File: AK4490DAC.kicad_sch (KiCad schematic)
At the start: 35 parts, among them IC1 LP5907MFX-3.3/NOPB, IC2 LP5907MFX-3.3/NOPB, IC3 LP5907MFX-3.3/NOPB, IC4 TPS7A2050PDBVR, IC5 MUSES8920, IC6 MUSES8920, IC7 MUSES8920, IC8 TPS7A2050PDBVR, IC9 AMS1117, J1 JST_XA_B02B-XASK-1, Q1 BSS138, T1 DA103C, U1 SN74LS06NSR, U3 TCM809RENB713, U4 TCM809RENB713, U5 AK4118, U6 AK4490, Y1 11.2896MHz

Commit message: Add PCM2704C USB input circuit with transformer isolation from AK4118
Places (unwired, matching this project's existing convention for
support components -- see the wiring table below) all parts needed for
the "SPDIF primary, USB via jumper" architecture:

PCM2704C USB Audio DAC (bus-powered, isolated USB-side domain):
- U2: PCM2704CDBR
- Y2 + C14/C15: 12MHz crystal w/ 22pF load caps (TI SBFS036A Fig.34)
- C16-C19: 1uF decoupling on VDD/VCCL/VCCR/VCCP
- C20: 10uF on VCOM
- R5: 1.5k D+ pullup to VCCP (full-speed device)
- R6/R7: 22R series termination on D+/D-
- J2: USB_B_Micro connector (VBUS/D+/D-/GND from USB, own USB_GND
  domain -- do NOT tie to main board GND)

Galvanic isolation network (reusing the already-placed T1/DA103C,
matching the original NEWDAC transformer-isolation topology):
- R8: 240R series from PCM2704C DOUT into T1 primary
- R9: 120R primary-side shunt/termination (USB_GND referenced)
- C21: 0.1uF DC block on T1 secondary
- R10: 75R secondary-side termination to main GND, mirroring the
  existing RX0 network's R2=75R (AK4118 datasheet Fig.21 pattern)

AK4118 RX channel select jumper:
- JP1: 3-pin header on IPS0 -- pin1=GND selects RX0 (external SPDIF
  input), pin3=+3V3_118 selects RX1 (PCM2704C via the isolation xfmr)

External SPDIF input jack:
- J3: 2-pin generic connector feeding the existing RX0 coupling
  network (C4/R2), placeholder footprint -- swap for the actual RCA
  or Toslink part footprint once chosen

New lib_symbols cache entries added: Connector_Generic:Conn_01x03,
Connector:USB_B_Micro (both extracted verbatim from KiCad's global
libraries, same safe methodology as the earlier LP5907/TPS7A20 fixes).

Bug found and fixed during this work: the Conn_01x03 block extracted
from the global library keeps its bare name ("Conn_01x03") instead of
the library-qualified name used by lib_id references
("Connector_Generic:Conn_01x03"). Instantiating a part against that
mismatched cache entry reproducibly segfaults kicad-cli sch erc --
same f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
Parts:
- added C14, C15: 22pF, Capacitor_SMD:C_0603_1608Metric, symbol Device:C
- added C16, C17, C18, C19: 1uF, Capacitor_SMD:C_0603_1608Metric, symbol Device:C
- added C20: 10uF, Capacitor_SMD:C_0805_2012Metric, symbol Device:C
- added C21: 0.1uF, Capacitor_SMD:C_0603_1608Metric, symbol Device:C
- added J2: USB_B_Micro, Connector_USB:USB_Micro-B_Molex-105017-0001, symbol Connector:USB_B_Micro
- added J3: SPDIF_IN, symbol Connector_Generic:Conn_01x02
- added JP1: IPS0_SEL, Connector_PinHeader_2.54mm:PinHeader_1x03_P2.54mm_Vertical, symbol Connector_Generic:Conn_01x03
- added R10: 75, Resistor_SMD:R_0603_1608Metric, symbol Device:R
- added R5: 1.5k, Resistor_SMD:R_0603_1608Metric, symbol Device:R
- added R6, R7: 22, Resistor_SMD:R_0603_1608Metric, symbol Device:R
- added R8: 240, Resistor_SMD:R_0603_1608Metric, symbol Device:R
- added R9: 120, Resistor_SMD:R_0603_1608Metric, symbol Device:R
- added U2: PCM2704CDBR, Package_SO:SSOP-28_5.3x10.2mm_P0.65mm, symbol AK4490DAC:PCM2704CDBR
- added Y2: 12MHz, Crystal:Crystal_SMD_3225-4Pin_3.2x2.5mm, symbol Device:Crystal

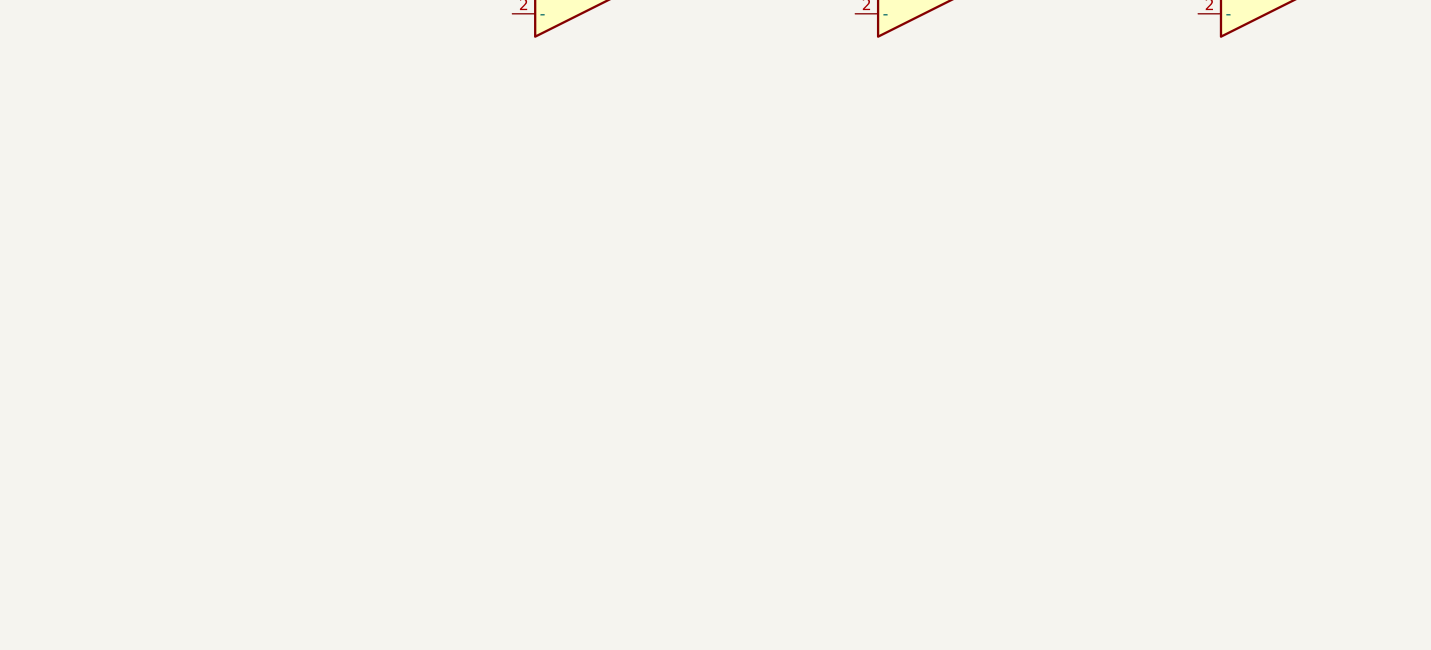
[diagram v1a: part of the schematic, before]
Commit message: Add AK4490 differential I/V + diff-amp output stage components
Places (unwired, per this project's convention) the analog output
stage feeding off the already-placed IC5/IC6/IC7 (MUSES8920 dual
op-amps) and Q1 (BSS138), using the AK4490's real differential current
output pins (AOUTLP/AOUTLN/VCML and AOUTRP/AOUTRN/VCMR, per the
pin-verified symbol) instead of a single-ended assumption.

Topology: 3 op-amp units per channel (I/V converter x2 + differential
combiner x1), which maps exactly onto the 3 existing dual-op-amp
packages:
  IC5 (A,B) -> L channel I/V converters (AOUTLP, AOUTLN)
  IC6 (A)   -> L channel differential-to-single-ended combiner
  IC6 (B)   -> R channel I/V converter (AOUTRP)
  IC7 (A)   -> R channel I/V converter (AOUTRN)
  IC7 (B)   -> R channel differential-to-single-ended combiner

New parts per channel:
- 2x 1k transimpedance feedback R (I/V conversion) + 2x 100pF parallel
  feedback C (HF stability)
- 4x 10k matched-resistor differential amplifier network (unity gain)
- 1x 1uF output DC-block coupling cap
- J4/J5: line-out connectors (L/R), placeholder footprint

Verified via kicad-cli sch erc: 377 violations, lib_symbol_mismatch=5
(unchanged baseline), no new violation categories, no crash.

Values (1k I/V, 100pF, 10k diff network, 1uF coupling) are reasonable
starting points, not simulated/verified against the AK4490 datasheet's
own reference application figure -- recommend double-checking against
that figure (output swing vs. AK4490's full-scale output current)
before finalizing for fab.

Still pending: net wiring for this stage and everything else placed so
far (left for manual wiring per this project's established pattern),
plus the remaining static AK4118/AK4490 mode-select pin ties.

Co-Authored-By: Claude Sonnet 5 <noreply@anthropic.com>
Claude-Session: https://claude.ai/code/session_01UHxU1bYnUhoAmCyc4Koj96
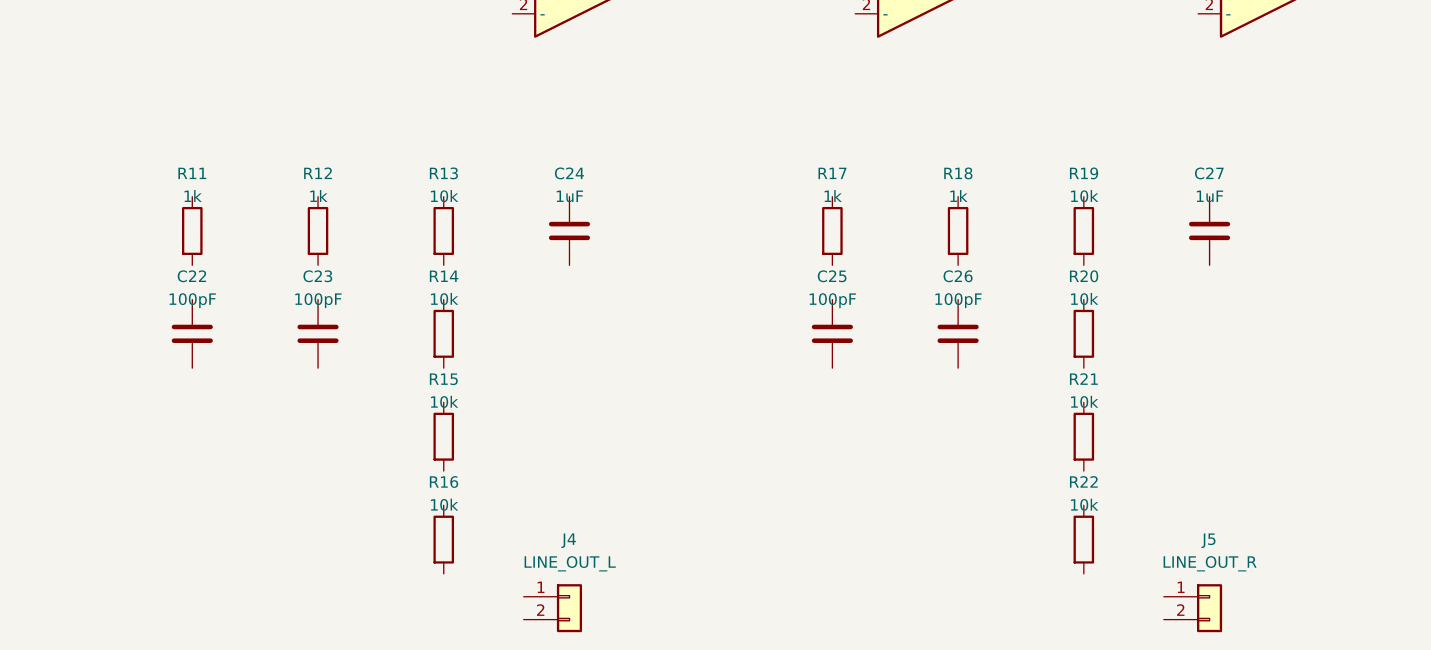
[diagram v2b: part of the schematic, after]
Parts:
- added C22, C23, C25, C26: 100pF, Capacitor_SMD:C_0603_1608Metric, symbol Device:C
- added C24, C27: 1uF, Capacitor_SMD:C_1206_3216Metric, symbol Device:C
- added J4: LINE_OUT_L, symbol Connector_Generic:Conn_01x02
- added J5: LINE_OUT_R, symbol Connector_Generic:Conn_01x02
- added R11, R12, R17, R18: 1k, Resistor_SMD:R_0603_1608Metric, symbol Device:R
- added R13, R14, R15, R16, R19, R20, R21, R22: 10k, Resistor_SMD:R_0603_1608Metric, symbol Device:R

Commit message: Fix reset supervisor (TCM809) threshold mismatch, add support parts
The TCM809RENB713 placed for U3 (AK4118 reset) and U4 (AK4490 reset)
back in the initial "upgrade" commit was never actually vetted against
Microchip's datasheet (DS21661E). This is a real orderable part (R =
2.55-2.70V threshold, ENB = SOT-23B marking code, both valid per the
datasheet's marking/ordering tables) -- but the R threshold grade is
specified by Microchip for 3.0V-nominal systems ("VDD = 3.3V for T/S,
3.0V for R" per the electrical characteristics table). Our AK4118/
AK4490 DVDD rails are 3.3V (from LP5907MFX-3.3), so R's ~2.63V typical
threshold would only assert reset once the 3.3V rail sagged over 20%,
well past the point the DACs are already out of spec (+-10% = 2.97V
floor). Changed both to TCM809TENB713 (T grade, 3.00-3.15V threshold,
the grade Microchip pairs with 3.3V-nominal systems), so reset holds
the chips down until VDD is back within their real operating range.

Also added, per the datasheet's own application notes that were
skipped originally:
- R25/R26: 100k pull-down from each TCM809's RESET output to GND
  (Sec 4.2 -- TCM809's RESET output goes high-Z below VDD=1.0V, so
  without this the AK4118/AK4490 PDN inputs would float during a deep
  power-down instead of being reliably held low)
- C28/C29: 0.1uF decoupling directly at each TCM809's VDD pin
  (Sec 4.1 -- improves transient/glitch immunity on the monitored rail)

Verified via kicad-cli sch erc: 385 violations, lib_symbol_mismatch=5
(unchanged baseline), no new violation categories, no crash.

TCM809 pinout (KiCad Power_Supervisor:TCM809, matches datasheet Table
3-1): pin1=GND, pin2=~RESET (active-low push-pull), pin3=VDD.
Wiring (still unwired, per this project's convention):
  U3: VDD->AK4118 DVDD rail, GND->main GND, RESET->AK4118 PDN (pin31)
  U4: VDD->AK4490 DVDD rail, GND->main GND, RESET->AK4490 PDN (pin2)
  R25/C28 at U3's RESET/VDD nodes; R26/C29 at U4's RESET/VDD nodes.

Co-Authored-By: Claude Sonnet 5 <n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
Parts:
- added C28, C29: 0.1uF, Capacitor_SMD:C_0603_1608Metric, symbol Device:C
- added R25, R26: 100k, Resistor_SMD:R_0603_1608Metric, symbol Device:R
- U3, U4: value TCM809RENB713 -> TCM809TENB713
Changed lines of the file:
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@@
 			)
 		)
-		(property "Value" "TCM809RENB713"
+		(property "Value" "TCM809TENB713"
 			(at 231.14 199.39 0)
 			(effects
@@
 			)
 		)
-		(property "Value" "TCM809RENB713"
+		(property "Value" "TCM809TENB713"
 			(at 269.24 199.39 0)
 			(effects
@@
 					(unit 1)
 				)
+			)
+		)
+	)
+	(symbol
+		(lib_id "Device:R")
+		(at 218.44 218.44 0)
+		(unit 1)
+		(exclude_from_sim no)
+		(in_bom yes)
+		(on_board yes)
+		(dnp no)
+		(property "Reference" "R25"
+			(at 218.44 212.09 0)
+			(effects (font (size 1.27 1.27)))
+		)
+		(property "Value" "100k"
+			(at 218.44 214.63 0)
+			(effects (font (size 1.27 1.27)))
+		)
+		(property "Footprint" "Resistor_SMD:R_0603_1608Metric"
+			(at 218.44 218.44 0)
+			(effects (font (size 1.27 1.27)) hide)
+		)
+		(property "Datasheet" ""
+			(at 218.44 218.44 0)
+			(effects (font (size 1.27 1.27)) hide)
+		)
+		(property "Description" "TCM809T (U3) RESET pull-down, datasheet Sec.4.2: keeps ~RESET valid down to VDD=0V"
+			(at 218.44 218.44 0)
+			(effects (font (size 1.27 1.27)) hide)
+		)
+		(pin "1"
+		)
+		(pin "2"
+		)
+		(instances
+			(project "AK4490DAC"
+				(path "/43171a2d-7dc9-4067-85e7-263b74d7a8f4"
+					(reference "R25")
+					(unit 1)
+				)
+			)
+		)
+	)
+	(symbol
+		(lib_id "Device:C")
+		(at 218.44 195.58 0)
+		(unit 1)
+		(exclude_from_sim no)
+		(in_bom yes)
+		(on_board yes)
+		(dnp no)
+		(property "Reference" "C28"
+			(at 218.44 189.23 0)
+			(effects (font (size 1.27 1.27)))
+		)
+		(property "Value" "0.1uF"
+			(at 218.44 191.77 0)
+			(effects (font (size 1.27 1.27)))
+		)
+		(property "Footprint" "Capacitor_SMD:C_0603_1608Metric"
+			(at 218.44 195.58 0)
+			(effects (font (size 1.27 1.27)) hide)
+		)
+		(property "Datasheet" ""
+			(at 218.44 195.58 0)
+			(effects (font (size 1.27 1.27)) hide)
+		)
+		(property "Description" "TCM809T (U3) VDD decoupling, datasheet Sec.4.1 transient immunity"
+			(at 218.44 195.58 0)
+			(effects (font (size 1.27 1.27)) hide)
+		)
+		(pin "1"
+		)
+		(pin "2"
+		)
+		(instances
+			(project "AK4490DAC"
+				(path "/43171a2d-7dc9-4067-85e7-263b74d7a8f4"
+					(reference "C28")
+					(unit 1)
+				)
+			)
+		)
+	)
+	(symbol
+		(lib_id "Device:R")
+		(at 281.94 218.44 0)
+		(unit 1)
+		(exclude_from_sim no)
+		(in_bom yes)
+		(on_board yes)
+		(dnp no)
+		(property "Reference" "R26"
+			(at 281.94 212.09 0)
+			(effects (font (size 1.27 1.27)))
+		)
+		(property "Value" "100k"
+			(at 281.94 214.63 0)
+			(effects (font (size 1.27 1.27)))
+		)
+		(property "Footprint" "Resistor_SMD:R_0603_1608Metric"
+			(at 281.94 218.44 0)
+			(effects (font (size 1.27 1.27)) hide)
+		)
+		(property "Datasheet" ""
+			(at 281.94 218.44 0)
+			(effects (font (size 1.27 1.27)) hide)
+		)
+		(property "Description" "TCM809T (U4) RESET pull-down, datasheet Sec.4.2: keeps ~RESET valid down to VDD=0V"
+			(at 281.94 218.44 0)
+			(effects (font (size 1.27 1.27)) hide)
+		)
+		(pin "1"
+		)
+		(pin "2"
+		)
+		(instances
+			(project "AK4490DAC"
+				(path "/43171a2d-7dc9-4067-85e7-263b74d7a8f4"
+					(reference "R26")
+					(unit 1)
+				)
+			)
+		)
+	)
+	(symbol
+		(lib_id "Device:C")
+		(at 281.94 195.58 0)
+		(unit 1)
+		(exclude_from_sim no)
+		(in_bom yes)
+		(on_board yes)
+		(dnp no)
+		(property "Reference" "C29"
+			(at 281.94 189.23 0)
+			(effects (font (size 1.27 1.27)))
+		)
+		(property "Value" "0.1uF"
+			(at 281.94 191.77 0)
+			(effects (font (size 1.27 1.27)))
+		)
+		(property "Footprint" "Capacitor_SMD:C_0603_1608Metric"
+			(at 281.94 195.58 0)
+			(effects (font (size 1.27 1.27)) hide)
+		)
+		(property "Datasheet" ""
+			(at 281.94 195.58 0)
+			(effects (font (size 1.27 1.27)) hide)
+		)
+		(property "Description" "TCM809T (U4) VDD decoupling, datasheet Sec.4.1 transient immunity"
+			(at 281.94 195.58 0)
+			(effects (font (size 1.27 1.27)) hide)
+		)
+		(pin "1"
+		)
+		(pin "2"
+		)
+		(instances
+			(project "AK4490DAC"
+				(path "/43171a2d-7dc9-4067-85e7-263b74d7a8f4"
+					(reference "C29")
+					(unit 1)
+				)
